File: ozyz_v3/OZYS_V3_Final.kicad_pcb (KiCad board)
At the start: 4 copper layers, 56 x 69 mm, 118 parts, among them CN1 532610571, J2 Conn_01x02_Pin, J3 AudioJack4, J4 AudioJack4, J5 AudioJack4, J6 AudioJack4, Q1 AO3400A, Q10 2N7002, Q2 AO3401A, Q3 2N7002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

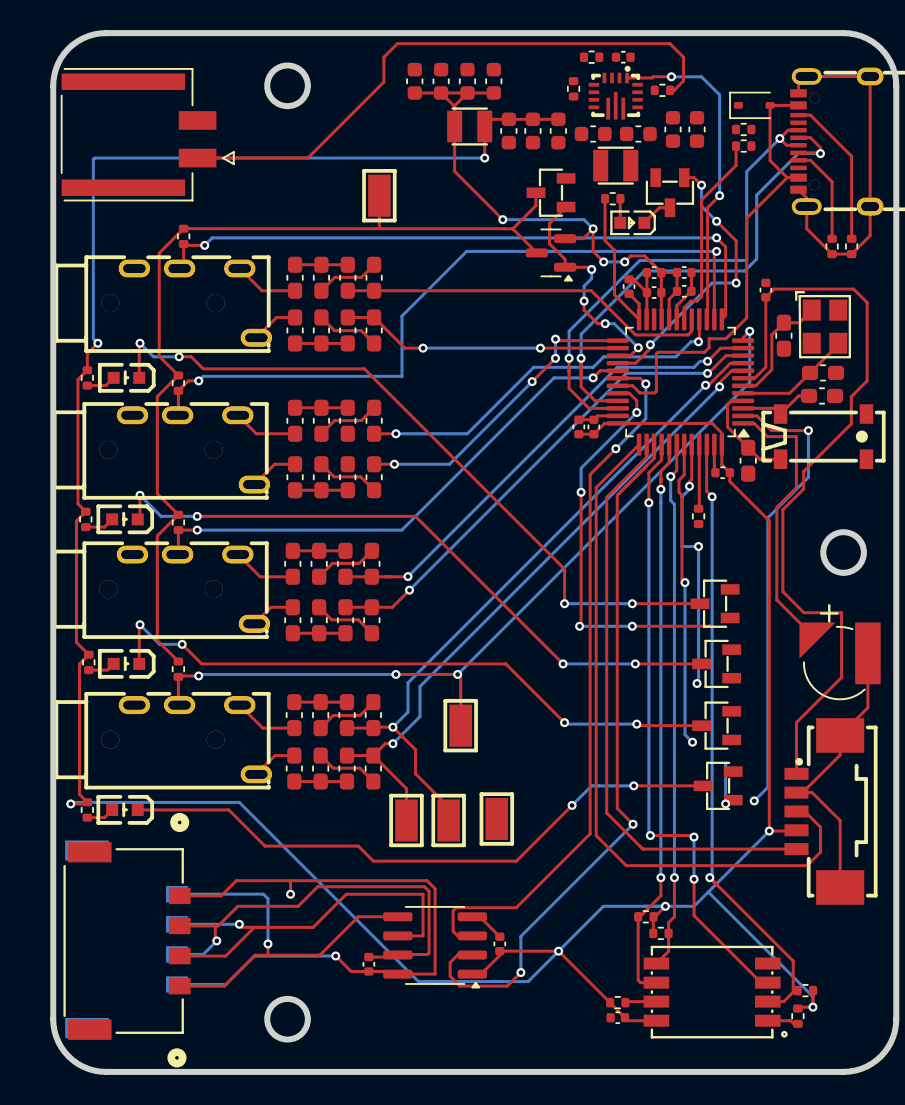
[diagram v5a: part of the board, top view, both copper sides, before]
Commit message: fixed connections and playing with pours
as summary describes
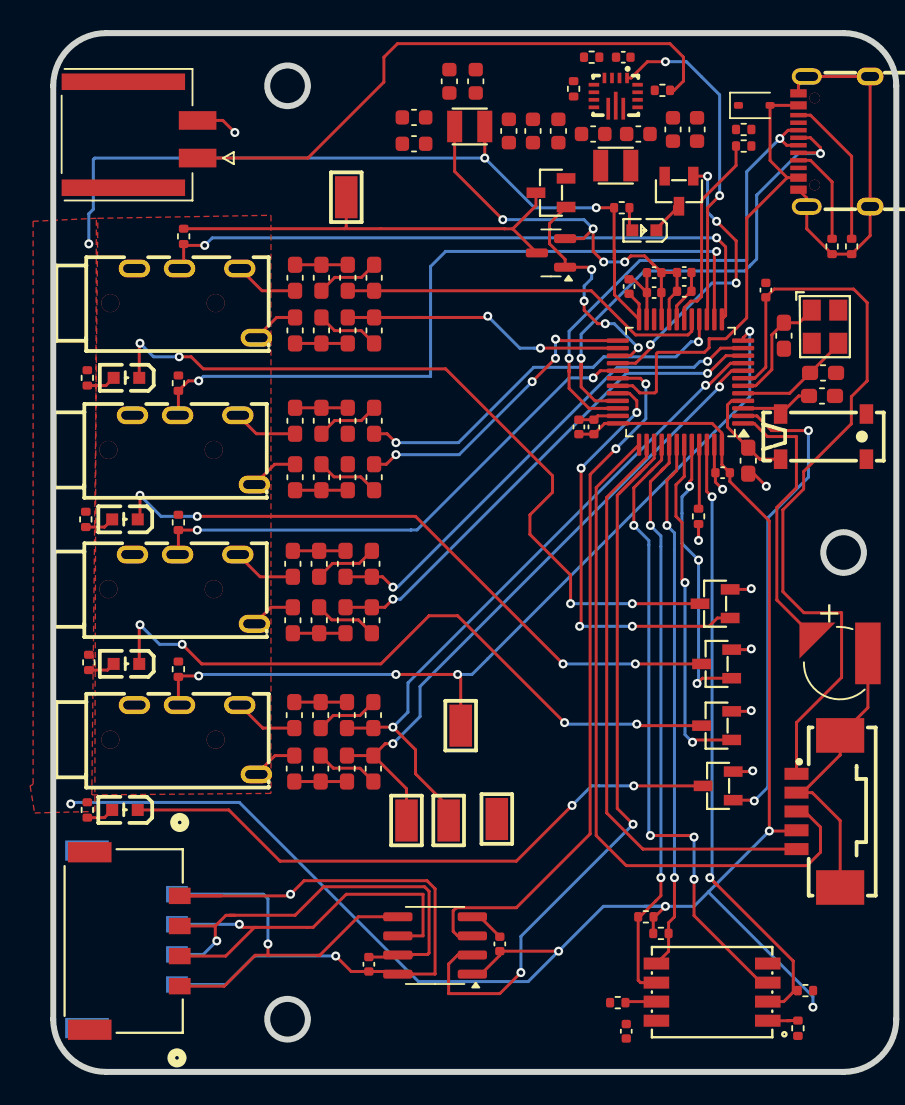
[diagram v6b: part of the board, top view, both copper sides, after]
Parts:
- moved C23 5.82 mm to (43.9, 24.1), turned to 0 degrees
- moved C25 5.46 mm to (43.9, 25.9), turned to 0 degrees
- moved C43 2.30 mm to (46.2, 21.7)
- moved C44 2.30 mm to (48.0, 21.7)
- moved U8 2.20 mm to (39.4, 29.4)
- moved C13 1.06 mm to (58.0, 84.8), turned to 90 degrees
- moved LED5 0.94 mm to (59.2, 31.6)
- moved R1 0.85 mm to (57.7, 30.1)
- moved R4 0.80 mm to (69.4, 84.6), turned to 90 degrees
- moved Q3 0.61 mm to (61.5, 29.0)
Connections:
- U2 pad 2: unconnected-(U2-PC13-Pad2) -> /LED1
- U2 pad 32: unconnected-(U2-PA10-Pad32) -> /LED2
- U2 pad 43: unconnected-(U2-PB6-Pad43) -> /LED4
- U2 pad 44: unconnected-(U2-PB7-Pad44) -> /LED3
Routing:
- net +3V3: track 216.3 -> 170.4 mm, vias 7 -> 8
- net 3V3A_SW: track 61.7 -> 29.3 mm
- net unconnected-(U2-PC13-Pad2): track 30.8 -> 0.00 mm, vias 2 -> 0
- net /LED1: track 2.80 -> 32.3 mm, vias 1 -> 2
- net /LED2: track 0.00 -> 28.3 mm, vias 0 -> 4
- net unconnected-(U2-PA10-Pad32): track 26.8 -> 0.00 mm, vias 4 -> 0
- net /LED4: track 0.00 -> 23.1 mm, vias 0 -> 2
- net unconnected-(U2-PB6-Pad43): track 20.3 -> 0.00 mm, vias 2 -> 0
- net /LED3: track 0.00 -> 19.1 mm, vias 0 -> 3
- net unconnected-(U2-PB7-Pad44): track 17.3 -> 0.00 mm, vias 3 -> 0
- net GND: track 92.8 -> 104.9 mm, vias 0 -> 8
- net +3V3A: track 41.8 -> 31.3 mm
- net Net-(LED1-K): track 48.2 -> 52.3 mm
- net Net-(LED4-K): track 42.7 -> 45.3 mm
- net /ONE_WIRE_OUT2: track 48.1 -> 50.1 mm
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- added copper zone on F.Cu, net +3V3
- added copper zone on F.Cu, net 3V3A_SW

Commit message: Test Config
Testing config :)
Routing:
- net +3V3: track 170.4 -> 144.1 mm
- net Net-(LED4-K): track 45.3 -> 42.7 mm, vias 4 -> 2
- net Net-(LED1-K): track 52.3 -> 51.0 mm, vias 4 -> 2
- net Net-(LED3-K): track 43.6 -> 42.9 mm, vias 4 -> 2
- net /LED1: track 32.3 -> 32.9 mm, vias 2 -> 3
- net /ONE_WIRE_OUT2: track 50.1 -> 49.6 mm
- net /DP3: track 19.5 -> 19.4 mm, vias 2 -> 0

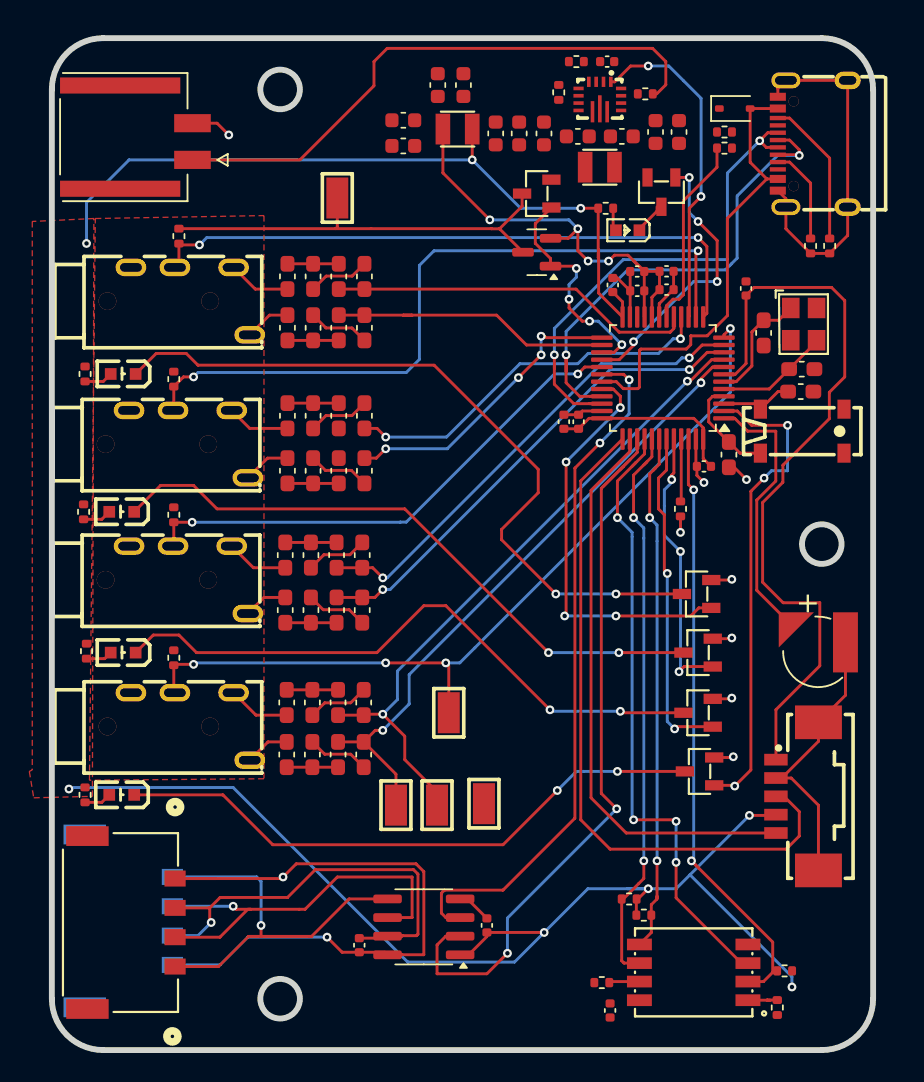
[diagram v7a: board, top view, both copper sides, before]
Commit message: Got rid of LED Fet
- restructuring
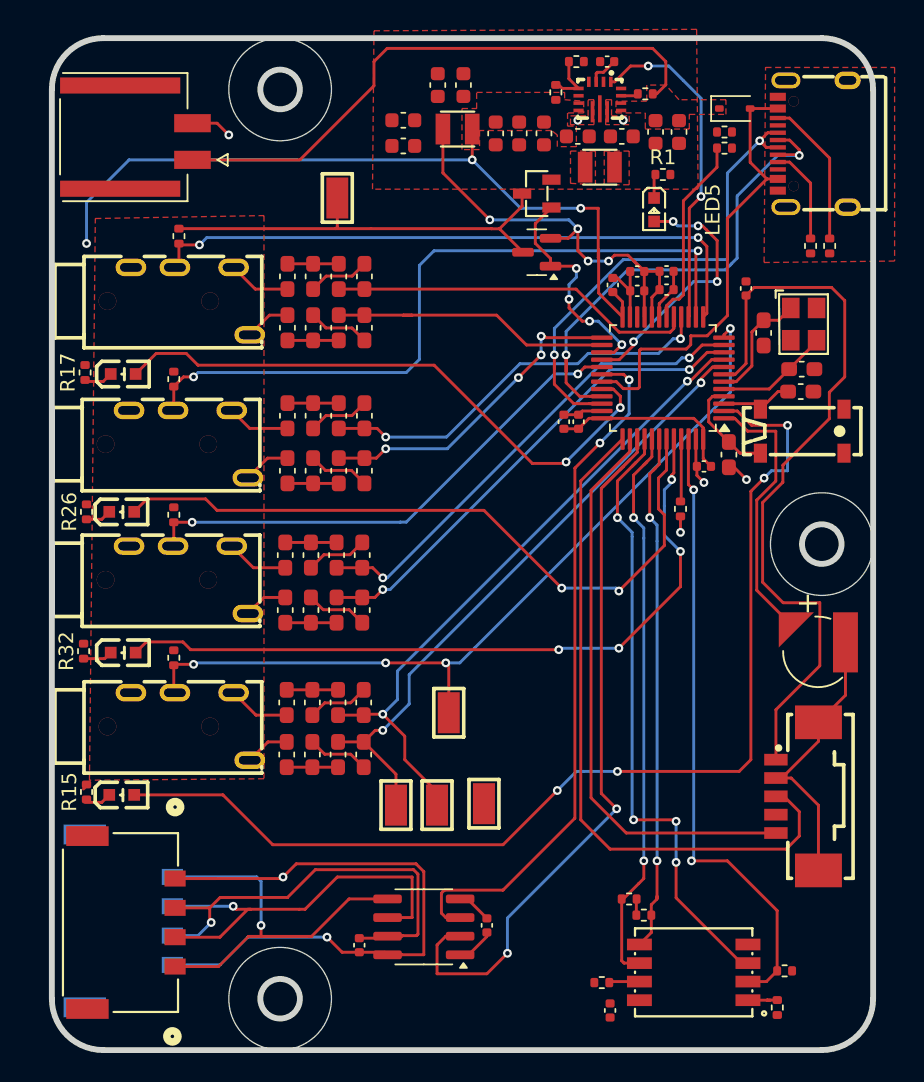
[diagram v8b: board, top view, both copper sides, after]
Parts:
- removed Q10, Q3, Q4, Q6, Q8: 2N7002, Rocketry_Easyeda:SOT-23-3_L2.9-W1.3-P1.90-LS2.4-BR
- R1: value 75R -> 220R
- R15, R17, R26, R32: value 33R -> 220R
- moved R1 4.53 mm to (61.6, 27.8)
- moved LED5 2.28 mm to (61.0, 30.2), turned to -90 degrees
- moved R15 0.22 mm to (22.3, 69.9), turned to 90 degrees
- moved R12 0.20 mm to (54.3, 22.2)
- moved R26 0.20 mm to (22.3, 50.8), turned to 90 degrees
- moved R32 0.20 mm to (22.1, 60.3), turned to 90 degrees
- moved R17 0.10 mm to (22.2, 41.3), turned to 90 degrees
- turned LED1 to 0 degrees
- turned LED2 to 0 degrees
- turned LED3 to 0 degrees
- turned LED4 to 0 degrees
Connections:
- LED1 pad 1: Net-(LED1-A) -> /LED2
- LED2 pad 1: Net-(LED2-A) -> /LED1
- LED3 pad 1: Net-(LED3-A) -> /LED3
- LED4 pad 1: Net-(LED4-A) -> /LED4
- LED5 pad 2: Net-(LED5-A) -> /STATUS_LED
- R1 pad 1: +3V3 -> Net-(LED5-C)
- R1 pad 2: Net-(LED5-A) -> GND
- R15 pad 1: +3V3 -> Net-(LED2-K)
- R15 pad 2: Net-(LED2-A) -> GND
- R17 pad 1: +3V3 -> Net-(LED1-K)
- R17 pad 2: Net-(LED1-A) -> GND
- R26 pad 1: +3V3 -> Net-(LED3-K)
- R26 pad 2: Net-(LED3-A) -> GND
- R32 pad 1: +3V3 -> Net-(LED4-K)
- R32 pad 2: Net-(LED4-A) -> GND
- U2 pad 43: /LED4 -> /LED3
- U2 pad 44: /LED3 -> /LED4
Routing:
- net +3V3: track 144.1 -> 69.7 mm, vias 8 -> 3
- net Net-(LED1-K): track 51.0 -> 1.96 mm, vias 2 -> 0
- net /LED1: track 32.9 -> 75.1 mm, vias 3 -> 4
- net Net-(LED3-K): track 42.9 -> 1.96 mm, vias 2 -> 0
- net Net-(LED4-K): track 42.7 -> 1.82 mm, vias 2 -> 0
- net Net-(LED2-K): track 41.0 -> 1.86 mm, vias 2 -> 0
- net GND: track 104.9 -> 75.3 mm, vias 8 -> 5
- net /LED3: track 19.1 -> 48.1 mm, vias 3 -> 2
- net /LED4: track 23.1 -> 50.2 mm, vias 2 -> 4
- net /LED2: track 28.3 -> 40.6 mm, vias 4 -> 2
- net Net-(U4-FB): track 0.00 -> 3.55 mm
- net Net-(U4-Vaux): track 0.00 -> 2.14 mm
- net Net-(LED3-A): track 1.96 -> 0.00 mm
- net Net-(LED1-A): track 1.96 -> 0.00 mm
- net Net-(LED2-A): track 1.86 -> 0.00 mm
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- added copper zone on F.Cu, net GND
- added copper zone on F.Cu, net Net-(D2-K)
- added copper zone on F.Cu, net Net-(U4-L1)
- added copper zone on F.Cu, net Net-(U4-L2)
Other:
- outline, holes or cut-outs redrawn
